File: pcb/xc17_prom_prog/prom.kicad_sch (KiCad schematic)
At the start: 28 parts, among them U15 SN74LVC8T245, U16 SN74LVC8T245, U17 SN74LVC8T245, U18 XC17xxx

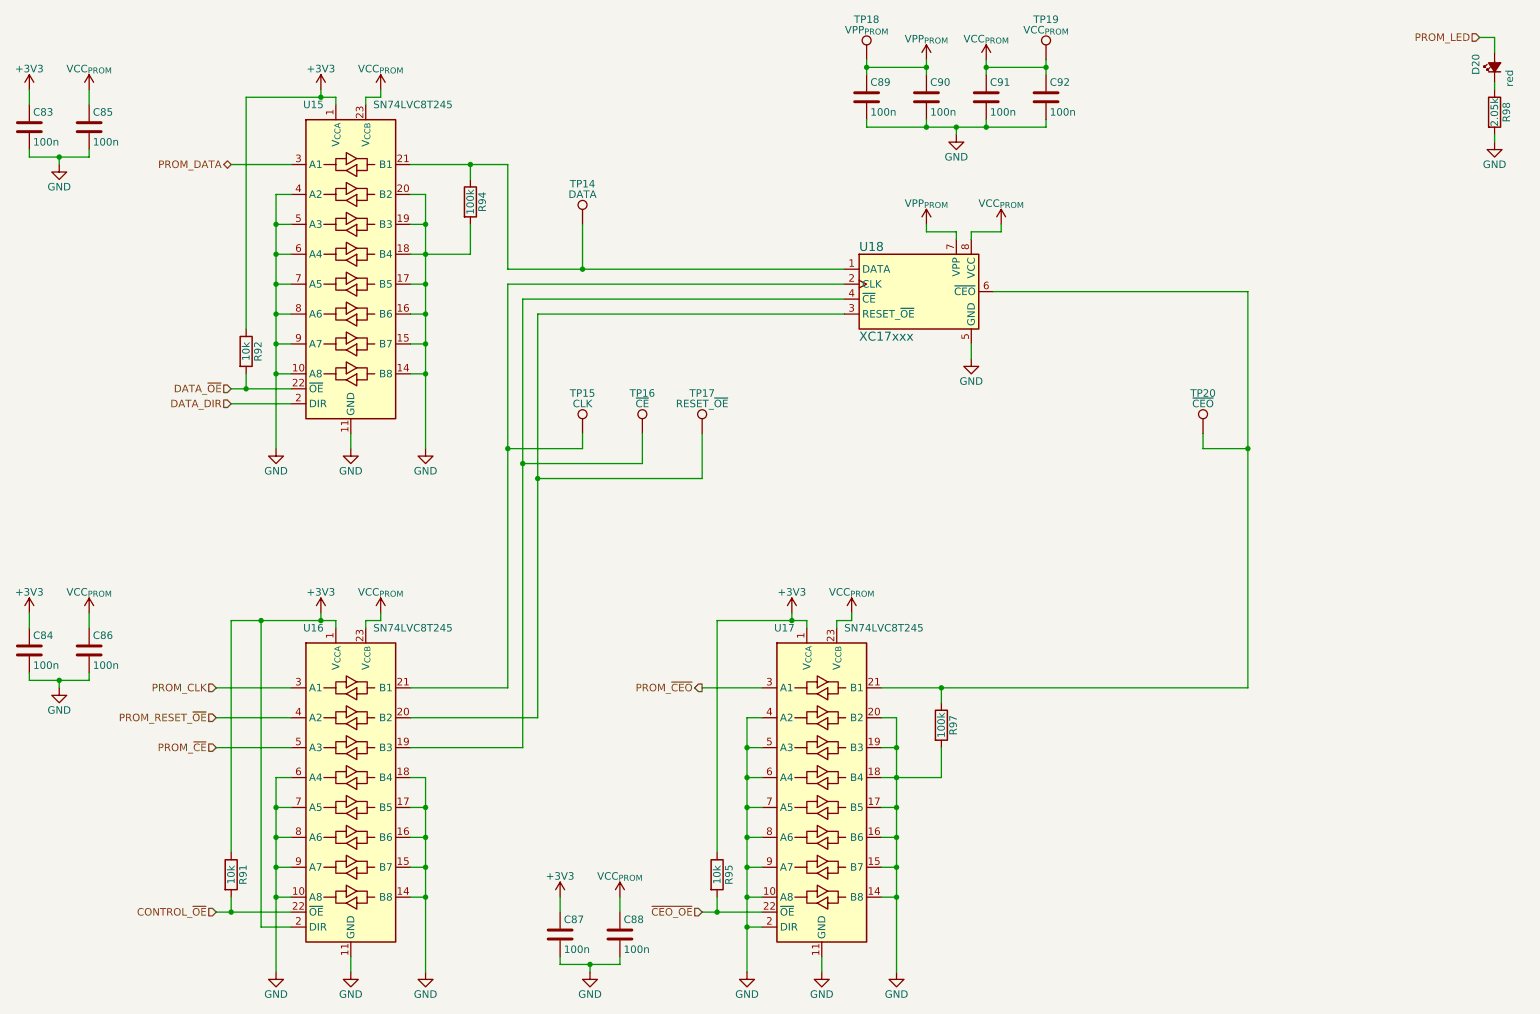
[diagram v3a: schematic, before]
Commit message: Migrate from HX1K to HX4K FPGA
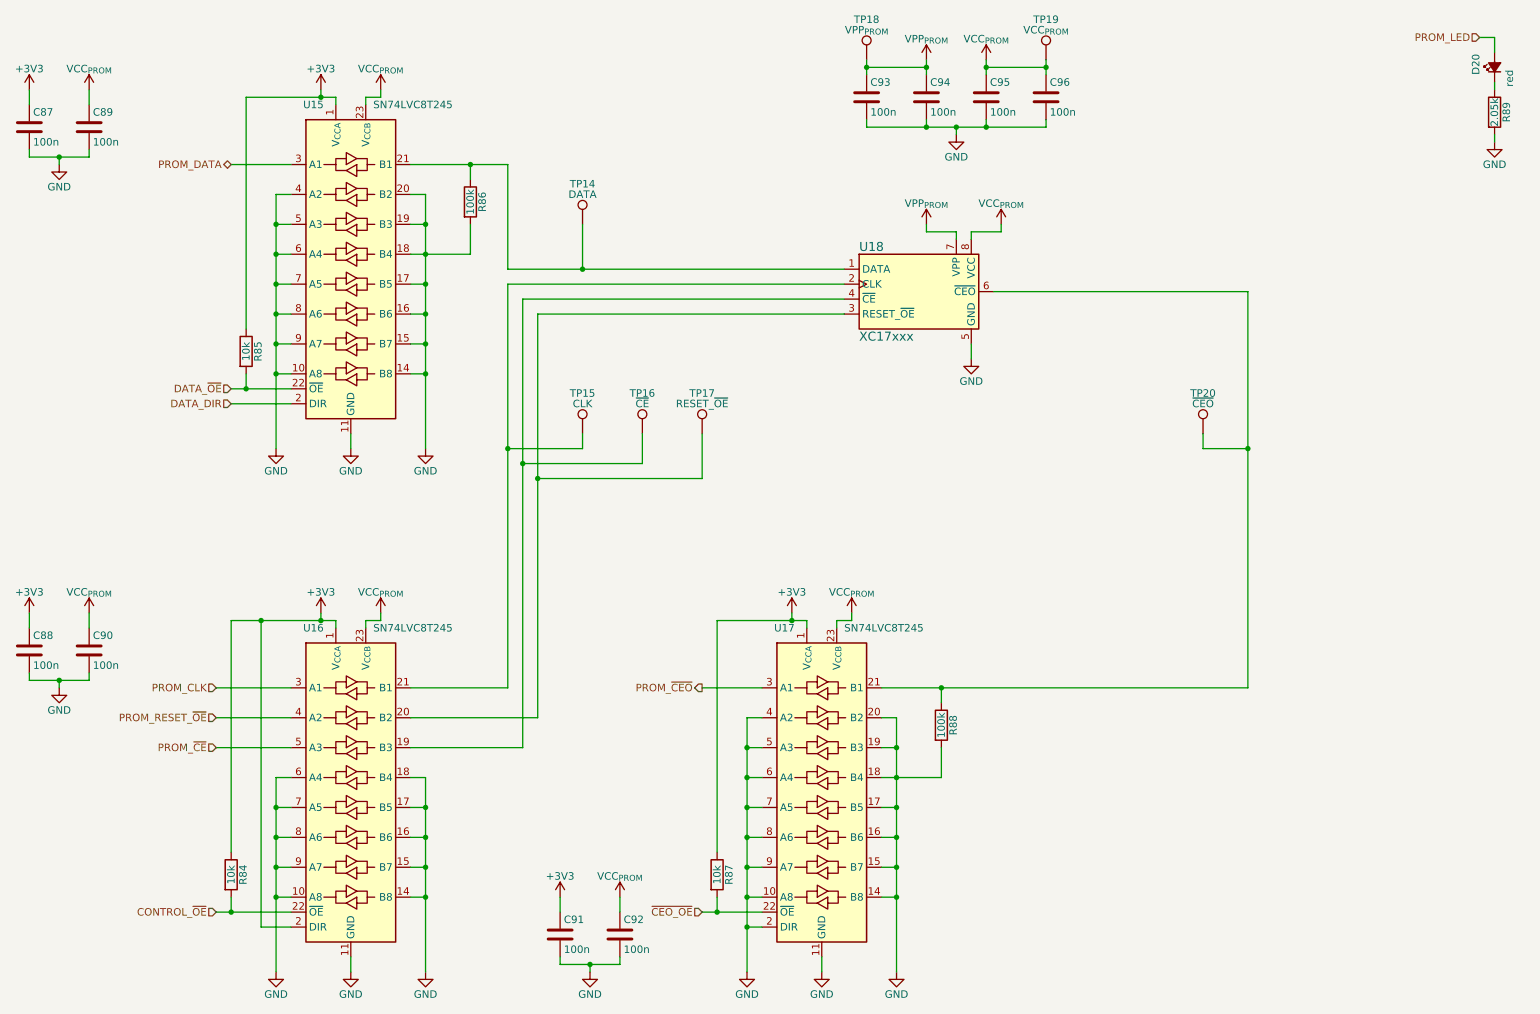
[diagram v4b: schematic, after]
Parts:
- renumbered C83 to C87, C84 to C88, C85 to C89, C86 to C90, C87 to C91, C88 to C92, C89 to C93, C90 to C94, C91 to C95, C92 to C96, R91 to R84, R92 to R85, R94 to R86, R95 to R87, R97 to R88, R98 to R89
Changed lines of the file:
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@@
 	(title_block
 		(title "XC17xxx PROM Programmer")
-		(date "2025-01-29")
+		(date "2025-01-30")
 		(rev "3")
 		(company "CC-BY-SA-4.0 Michael Singer")
@@
 		(on_board yes)
 		(dnp no)
-		(property "Reference" "C91"
+		(property "Reference" "C95"
 			(at 180.975 29.21 0)
 			(effects
@@
 			(project "xc17_prom_prog"
 				(path "/3afea672-343d-4fc8-b012-067ac21cc0e9/43172acb-73d1-430e-bac0-31c53bbc6dab"
-					(reference "C91")
+					(reference "C95")
 					(unit 1)
 				)
@@
 		(on_board yes)
 		(dnp no)
-		(property "Reference" "C89"
+		(property "Reference" "C93"
 			(at 160.655 29.21 0)
 			(effects
@@
 			(project "xc17_prom_prog"
 				(path "/3afea672-343d-4fc8-b012-067ac21cc0e9/43172acb-73d1-430e-bac0-31c53bbc6dab"
-					(reference "C89")
+					(reference "C93")
 					(unit 1)
 				)
@@
 		(on_board yes)
 		(dnp no)
-		(property "Reference" "R91"
+		(property "Reference" "R84"
 			(at 54.102 163.83 90)
 			(effects
@@
 			(project ""
 				(path "/3afea672-343d-4fc8-b012-067ac21cc0e9/43172acb-73d1-430e-bac0-31c53bbc6dab"
-					(reference "R91")
+					(reference "R84")
 					(unit 1)
 				)
@@
 		(on_board yes)
 		(dnp no)
-		(property "Reference" "C90"
+		(property "Reference" "C94"
 			(at 170.815 29.21 0)
 			(effects
@@
 			(project "xc17_prom_prog"
 				(path "/3afea672-343d-4fc8-b012-067ac21cc0e9/43172acb-73d1-430e-bac0-31c53bbc6dab"
-					(reference "C90")
+					(reference "C94")
 					(unit 1)
 				)
@@
 		(on_board yes)
 		(dnp no)
-		(property "Reference" "R94"
+		(property "Reference" "R86"
 			(at 94.742 49.53 90)
 			(effects
@@
 			(project "xc17_prom_prog"
 				(path "/3afea672-343d-4fc8-b012-067ac21cc0e9/43172acb-73d1-430e-bac0-31c53bbc6dab"
-					(reference "R94")
+					(reference "R86")
 					(unit 1)
 				)
@@
 		(on_board yes)
 		(dnp no)
-		(property "Reference" "R95"
+		(property "Reference" "R87"
 			(at 136.652 163.83 90)
 			(effects
@@
 			(project "xc17_prom_prog"
 				(path "/3afea672-343d-4fc8-b012-067ac21cc0e9/43172acb-73d1-430e-bac0-31c53bbc6dab"
-					(reference "R95")
+					(reference "R87")
 					(unit 1)
 				)
@@
 		(on_board yes)
 		(dnp no)
-		(property "Reference" "R97"
+		(property "Reference" "R88"
 			(at 174.752 138.43 90)
 			(effects
@@
 			(project "xc17_prom_prog"
 				(path "/3afea672-343d-4fc8-b012-067ac21cc0e9/43172acb-73d1-430e-bac0-31c53bbc6dab"
-					(reference "R97")
+					(reference "R88")
 					(unit 1)
 				)
@@
 		(on_board yes)
 		(dnp no)
-		(property "Reference" "C92"
+		(property "Reference" "C96"
 			(at 191.135 29.21 0)
 			(effects
@@
 			(project "xc17_prom_prog"
 				(path "/3afea672-343d-4fc8-b012-067ac21cc0e9/43172acb-73d1-430e-bac0-31c53bbc6dab"
-					(reference "C92")
+					(reference "C96")
 					(unit 1)
 				)
@@
 		(on_board yes)
 		(dnp no)
-		(property "Reference" "C88"
+		(property "Reference" "C92"
 			(at 118.745 171.45 0)
 			(effects
@@
 			(project "xc17_prom_prog"
 				(path "/3afea672-343d-4fc8-b012-067ac21cc0e9/43172acb-73d1-430e-bac0-31c53bbc6dab"
-					(reference "C88")
+					(reference "C92")
 					(unit 1)
 				)
@@
 		(on_board yes)
 		(dnp no)
-		(property "Reference" "C84"
+		(property "Reference" "C88"
 			(at 18.415 123.19 0)
 			(effects
@@
 			(project "xc17_prom_prog"
 				(path "/3afea672-343d-4fc8-b012-067ac21cc0e9/43172acb-73d1-430e-bac0-31c53bbc6dab"
-					(reference "C84")
+					(reference "C88")
 					(unit 1)
 				)
@@
 		(on_board yes)
 		(dnp no)
-		(property "Reference" "R98"
+		(property "Reference" "R89"
 			(at 268.732 34.29 90)
 			(effects
@@
 			(project "xc17_prom_prog"
 				(path "/3afea672-343d-4fc8-b012-067ac21cc0e9/43172acb-73d1-430e-bac0-31c53bbc6dab"
-					(reference "R98")
+					(reference "R89")
 					(unit 1)
 				)
@@
 		(on_board yes)
 		(dnp no)
-		(property "Reference" "C85"
+		(property "Reference" "C89"
 			(at 28.575 34.29 0)
 			(effects
@@
 			(project "xc17_prom_prog"
 				(path "/3afea672-343d-4fc8-b012-067ac21cc0e9/43172acb-73d1-430e-bac0-31c53bbc6dab"
-					(reference "C85")
+					(reference "C89")
 					(unit 1)
 				)
@@
 		(on_board yes)
 		(dnp no)
-		(property "Reference" "C87"
+		(property "Reference" "C91"
 			(at 108.585 171.45 0)
 			(effects
@@
 			(project "xc17_prom_prog"
 				(path "/3afea672-343d-4fc8-b012-067ac21cc0e9/43172acb-73d1-430e-bac0-31c53bbc6dab"
-					(reference "C87")
+					(reference "C91")
 					(unit 1)
 				)
@@
 		(on_board yes)
 		(dnp no)
-		(property "Reference" "C86"
+		(property "Reference" "C90"
 			(at 28.575 123.19 0)
 			(effects
@@
 			(project "xc17_prom_prog"
 				(path "/3afea672-343d-4fc8-b012-067ac21cc0e9/43172acb-73d1-430e-bac0-31c53bbc6dab"
-					(reference "C86")
+					(reference "C90")
 					(unit 1)
 				)
@@
 		(on_board yes)
 		(dnp no)
-		(property "Reference" "R92"
+		(property "Reference" "R85"
 			(at 56.642 74.93 90)
 			(effects
@@
 			(project "xc17_prom_prog"
 				(path "/3afea672-343d-4fc8-b012-067ac21cc0e9/43172acb-73d1-430e-bac0-31c53bbc6dab"
-					(reference "R92")
+					(reference "R85")
 					(unit 1)
 				)
@@
 		(on_board yes)
 		(dnp no)
-		(property "Reference" "C83"
+		(property "Reference" "C87"
 			(at 18.415 34.29 0)
 			(effects
@@
 			(project "xc17_prom_prog"
 				(path "/3afea672-343d-4fc8-b012-067ac21cc0e9/43172acb-73d1-430e-bac0-31c53bbc6dab"
-					(reference "C83")
+					(reference "C87")
 					(unit 1)
 				)
